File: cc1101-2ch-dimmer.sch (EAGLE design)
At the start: 26 parts, among them Q1 IRLZ44NS, Q2 IRLZ44NS, U1 ATMEGA328P-AU, U2 0ZCG0035AF2C, U3 173950378, X2 MSTBA2, X3 MSTBA2, X4 MSTBA2, Y1 CSTCE8M00G52

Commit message: added info to schematic
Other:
- note added: "cod.m GmbH 2019 Patrik Mayer codm.de, CC-BY-NC"
- note removed: "CC-BY-NC codm.de, 2019"
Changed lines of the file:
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@@
 <sheet>
 <plain>
-<text x="86.36" y="111.76" size="3.302" layer="97">CC-BY-NC
-codm.de, 2019</text>
+<text x="164.338" y="21.844" size="2.54" layer="94" align="top-left">cod.m GmbH 2019
+Patrik Mayer
+codm.de, CC-BY-NC</text>
 </plain>
 <instances>

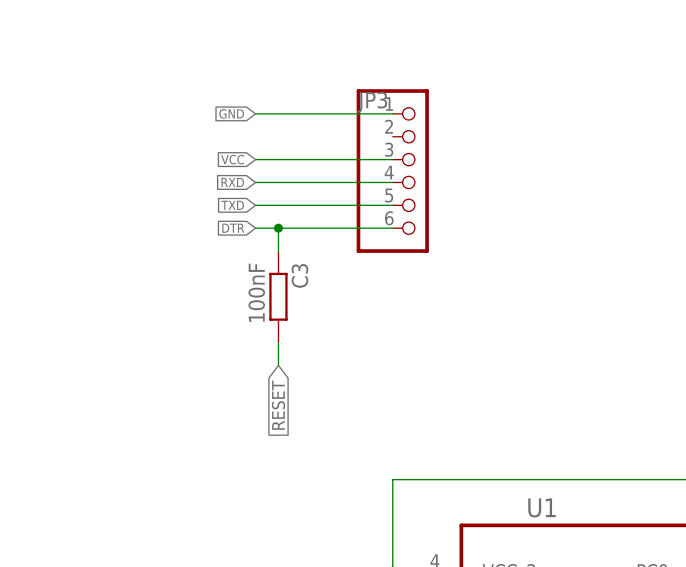
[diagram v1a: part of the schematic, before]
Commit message: fixed wrong symbol for C3
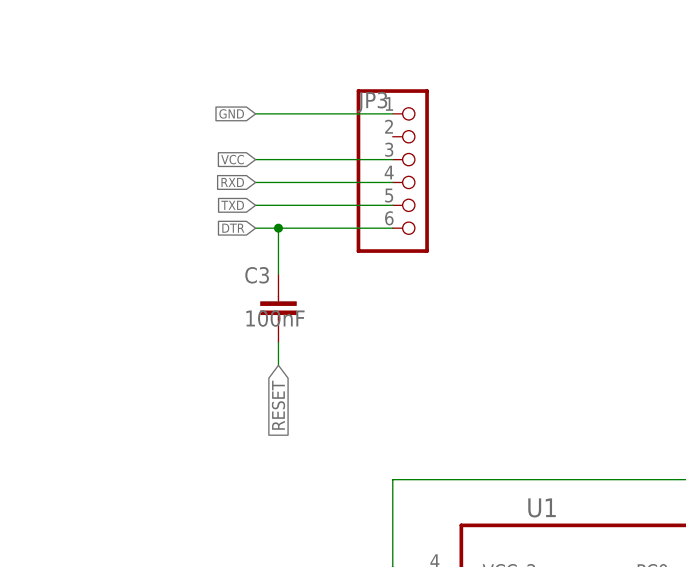
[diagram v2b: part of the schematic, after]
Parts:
- C3: device rcl:R-EU_R0805 -> rcl:C-EUC0805
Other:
- moved on the sheet: C3
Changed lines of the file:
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@@
 <part name="X1" library="adafruit" library_urn="urn:adsk.eagle:library:420" deviceset="ANTENNA_U.FL" device="" package3d_urn="urn:adsk.eagle:package:6240943/1" override_package3d_urn="urn:adsk.eagle:package:11204466/2" override_package_urn="urn:adsk.eagle:footprint:6240300/1"/>
 <part name="JP3" library="pinhead" library_urn="urn:adsk.eagle:library:325" deviceset="PINHD-1X6" device="" package3d_urn="urn:adsk.eagle:package:22472/2"/>
-<part name="C3" library="rcl" library_urn="urn:adsk.eagle:library:334" deviceset="R-EU_" device="R0805" package3d_urn="urn:adsk.eagle:package:23553/2" value="100nF"/>
+<part name="C3" library="rcl" library_urn="urn:adsk.eagle:library:334" deviceset="C-EU" device="C0805" package3d_urn="urn:adsk.eagle:package:23617/2" value="100nF"/>
 <part name="Q1" library="codm" library_urn="urn:adsk.eagle:library:11602856" deviceset="IRLZ44NS" device="D2PAK" package3d_urn="urn:adsk.eagle:package:11744053/3" value="IRLZ44NS"/>
 <part name="Q2" library="codm" library_urn="urn:adsk.eagle:library:11602856" deviceset="IRLZ44NS" device="D2PAK" package3d_urn="urn:adsk.eagle:package:11744053/3" value="IRLZ44NS"/>
@@
 <attribute name="VALUE" x="49.53" y="114.3" size="1.778" layer="96"/>
 </instance>
-<instance part="C3" gate="G$1" x="40.64" y="111.76" smashed="yes" rot="R270">
-<attribute name="NAME" x="42.1386" y="115.57" size="1.778" layer="95" rot="R270"/>
-<attribute name="VALUE" x="37.338" y="115.57" size="1.778" layer="96" rot="R270"/>
+<instance part="C3" gate="G$1" x="40.64" y="111.76" smashed="yes">
+<attribute name="NAME" x="36.83" y="113.2586" size="1.778" layer="95"/>
+<attribute name="VALUE" x="36.83" y="108.458" size="1.778" layer="96"/>
 </instance>
 <instance part="Q1" gate="G$1" x="226.06" y="78.74" smashed="yes">
@@
 <pinref part="C3" gate="G$1" pin="1"/>
 <wire x1="40.64" y1="119.38" x2="38.1" y2="119.38" width="0.1524" layer="91"/>
-<wire x1="40.64" y1="116.84" x2="40.64" y2="119.38" width="0.1524" layer="91"/>
+<wire x1="40.64" y1="114.3" x2="40.64" y2="119.38" width="0.1524" layer="91"/>
 <junction x="40.64" y="119.38"/>
 <pinref part="JP3" gate="A" pin="6"/>
